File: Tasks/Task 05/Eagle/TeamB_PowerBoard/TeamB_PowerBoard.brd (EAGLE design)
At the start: 100 x 63.5 mm, 35 parts

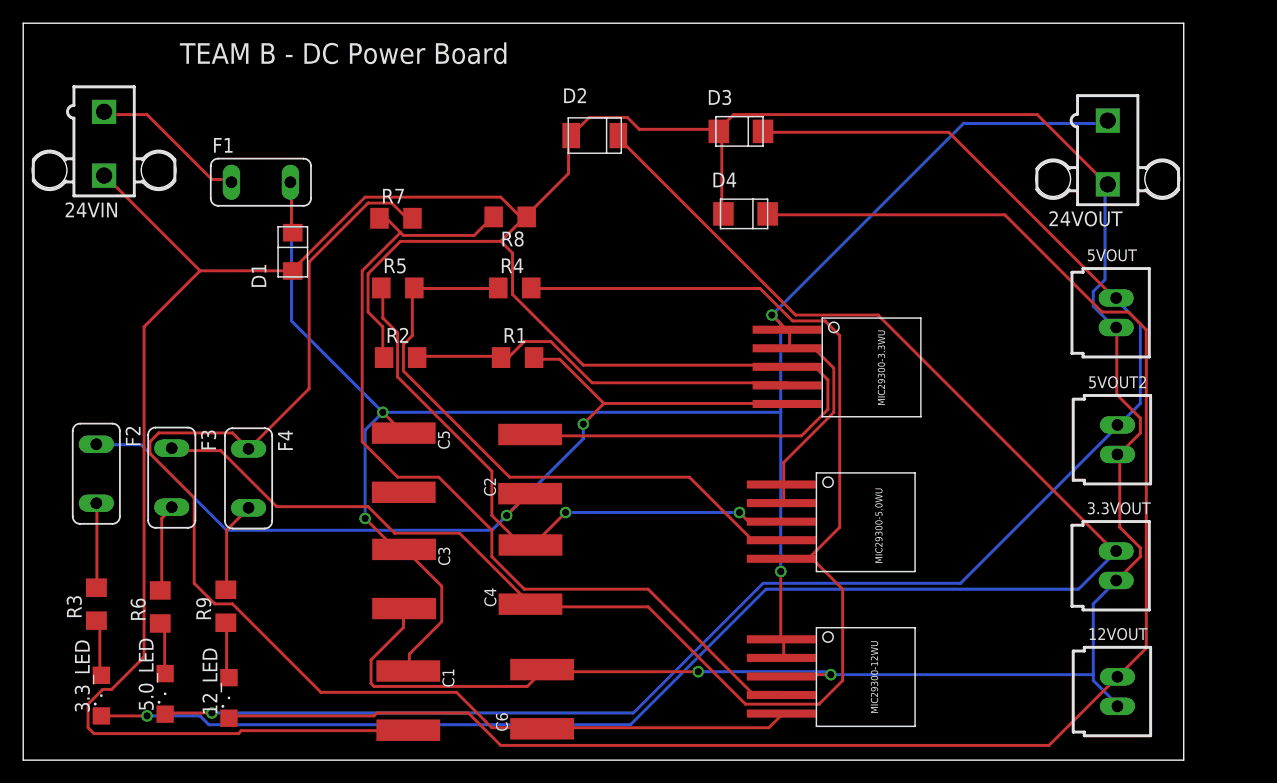
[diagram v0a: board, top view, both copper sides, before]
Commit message: Added the 4 holes to the PCB
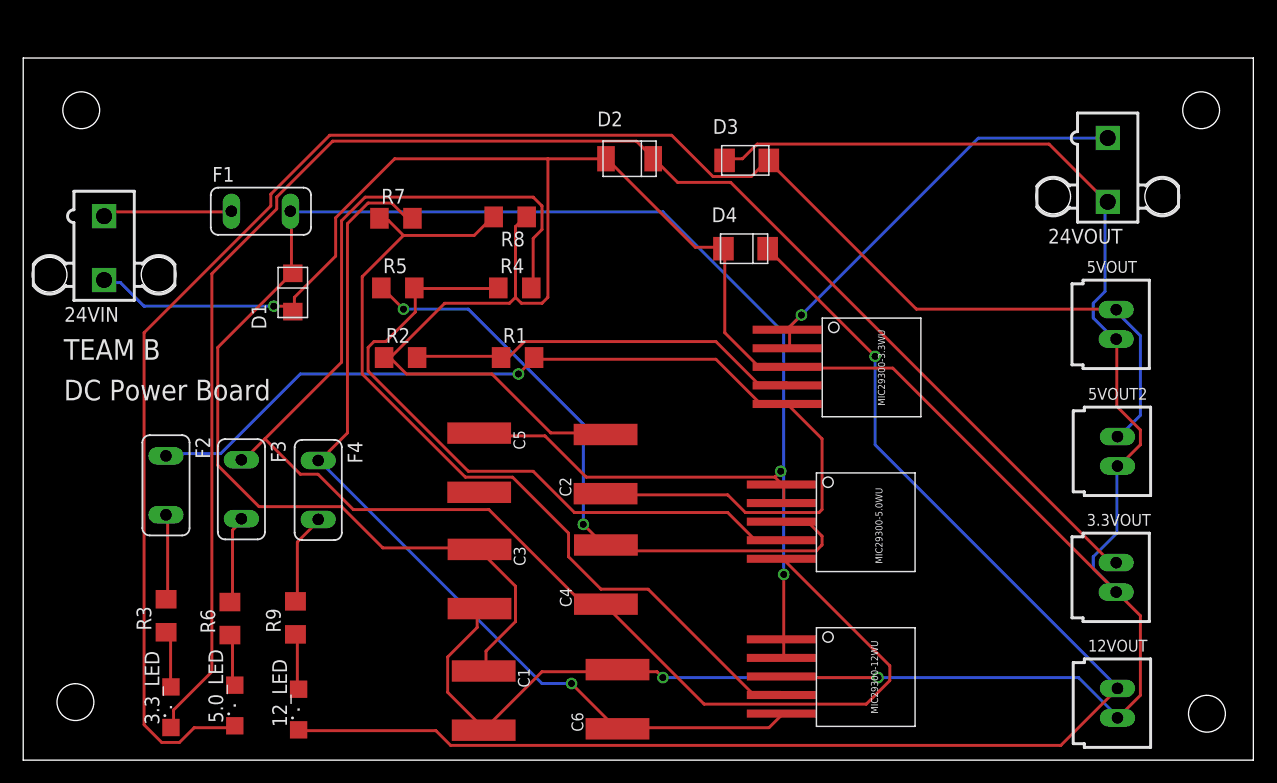
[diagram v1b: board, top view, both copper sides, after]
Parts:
- moved 24VIN 9.00 mm to (6.97, 44.1)
- moved C1 6.50 mm to (39.7, 5.13)
- moved C2 6.50 mm to (50.2, 25.5)
- moved C3 6.50 mm to (39.3, 15.6)
- moved C4 6.50 mm to (50.2, 16.0)
- moved C5 6.50 mm to (39.3, 25.6)
- moved C6 6.50 mm to (51.2, 5.25)
- moved F2 6.08 mm to (12.3, 23.7)
- moved R3 6.08 mm to (12.3, 12.4)
- moved 12_LED 6.08 mm to (23.7, 4.36)
- moved 3.3_LED 6.08 mm to (12.7, 4.56)
- moved 5.0_LED 6.08 mm to (18.2, 4.71)
- moved F3 6.08 mm to (18.8, 23.3)
- moved F4 6.08 mm to (25.4, 23.3)
- moved R6 6.08 mm to (17.8, 12.2)
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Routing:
- net GND: track 396.0 -> 341.0 mm, vias 2 -> 3
- net N$8: track 109.4 -> 78.5 mm, vias 0 -> 1
- net N$1: track 180.0 -> 207.6 mm, vias 4 -> 3
- net N$18: track 148.1 -> 123.5 mm, vias 0 -> 1
- net N$9: track 151.8 -> 138.9 mm, vias 1 -> 0
- net N$15: track 141.5 -> 154.3 mm, vias 1 -> 0
- net N$5: track 78.3 -> 88.5 mm, vias 2 -> 1
- net N$6: track 51.1 -> 57.5 mm
- net N$13: track 53.5 -> 58.3 mm
- net N$7: track 133.0 -> 128.8 mm
- net N$19: track 77.2 -> 73.5 mm
- net VCC: track 13.6 -> 11.1 mm
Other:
- board size 100 x 63.5 mm -> 106 x 60.5 mm
- board text added: "DC Power Board"
- board text added: "TEAM B"
- board text removed: "TEAM B - DC Power Board"

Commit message: Added 4th LED
Added 4th LED to PCB and Schematic
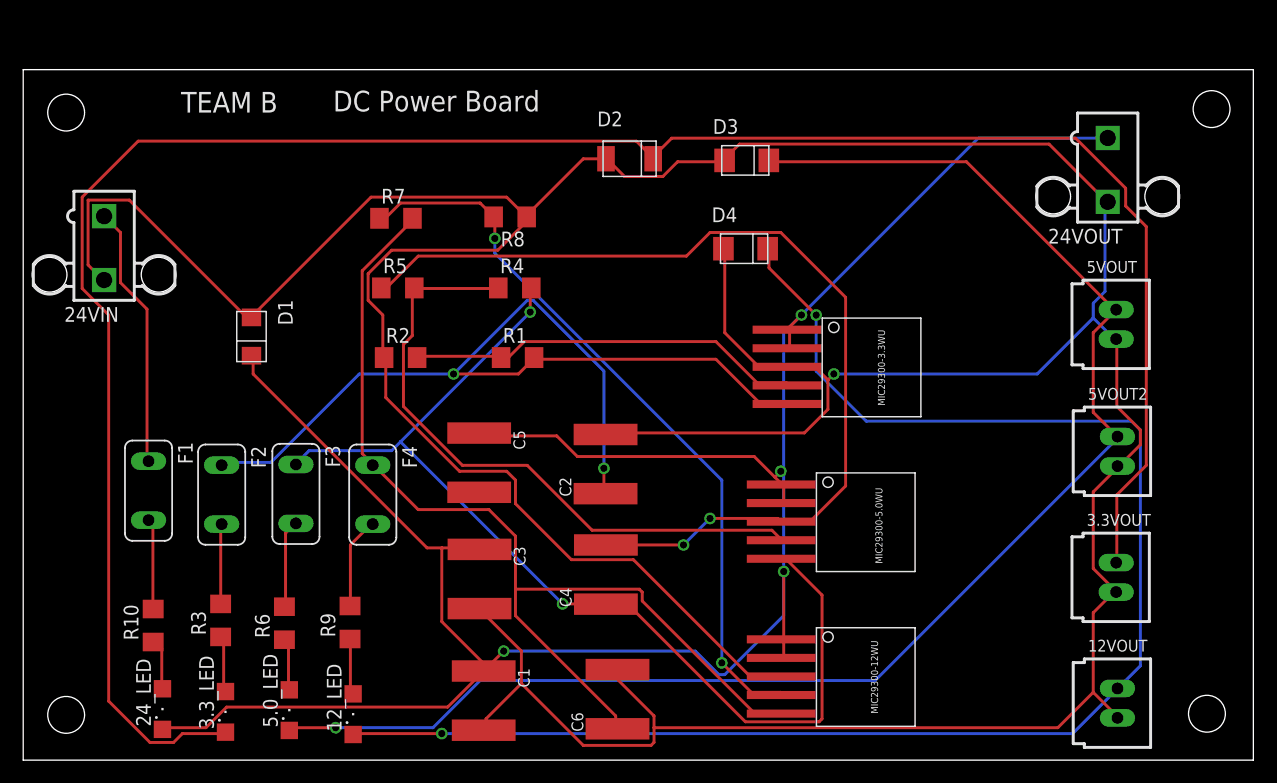
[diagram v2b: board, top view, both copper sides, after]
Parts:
- added 24_LED: (no value), led:SML1206
- added R10: 2.2K, rcl:R1206
- moved F1 26.0 mm to (10.8, 23.2), turned to 270 degrees
- moved F2 4.87 mm to (17.1, 22.9)
- moved R6 4.72 mm to (22.5, 11.8)
- moved R3 4.72 mm to (17.0, 12.0)
- moved 12_LED 4.72 mm to (28.4, 3.96)
- moved 3.3_LED 4.72 mm to (17.4, 4.16)
- moved 5.0_LED 4.72 mm to (22.9, 4.31)
- moved F3 4.72 mm to (23.5, 22.9)
- moved F4 4.72 mm to (30.1, 22.9)
- moved R9 4.72 mm to (28.2, 11.9)
- moved D1 4.09 mm to (19.7, 37.4), turned to 270 degrees
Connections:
- new net N$10: F1.2, R10.2
- new net N$20: 24_LED.A, R10.1
- net N$1: now also 24_LED.C; no longer F1.2
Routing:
- net N$9: track 138.9 -> 185.5 mm
- net N$7: track 128.8 -> 89.9 mm, vias 0 -> 2
- net GND: track 341.0 -> 373.6 mm, vias 3 -> 1
- net N$6: track 57.5 -> 83.6 mm
- net N$15: track 154.3 -> 129.9 mm, vias 0 -> 1
- net VCC: track 11.1 -> 22.7 mm
- net N$19: track 73.5 -> 63.8 mm, vias 0 -> 2
- net N$18: track 123.5 -> 133.0 mm, vias 1 -> 2
- net N$8: track 78.5 -> 86.3 mm, vias 1 -> 0
- net N$10: track 0.00 -> 7.82 mm
- net N$1: track 207.6 -> 200.2 mm, vias 3 -> 4
- net N$5: track 88.5 -> 83.0 mm, vias 1 -> 2
- net N$20: track 0.00 -> 4.46 mm
- net N$13: track 58.3 -> 55.3 mm
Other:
- board size 106 x 60.5 mm -> 106 x 59.5 mm

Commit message: Fixed Libraries and Wiring
Fixed the Library components to reflect DIP variants.
Fixed schematic for LED wiring.
ERC passes for both PCB and SCH
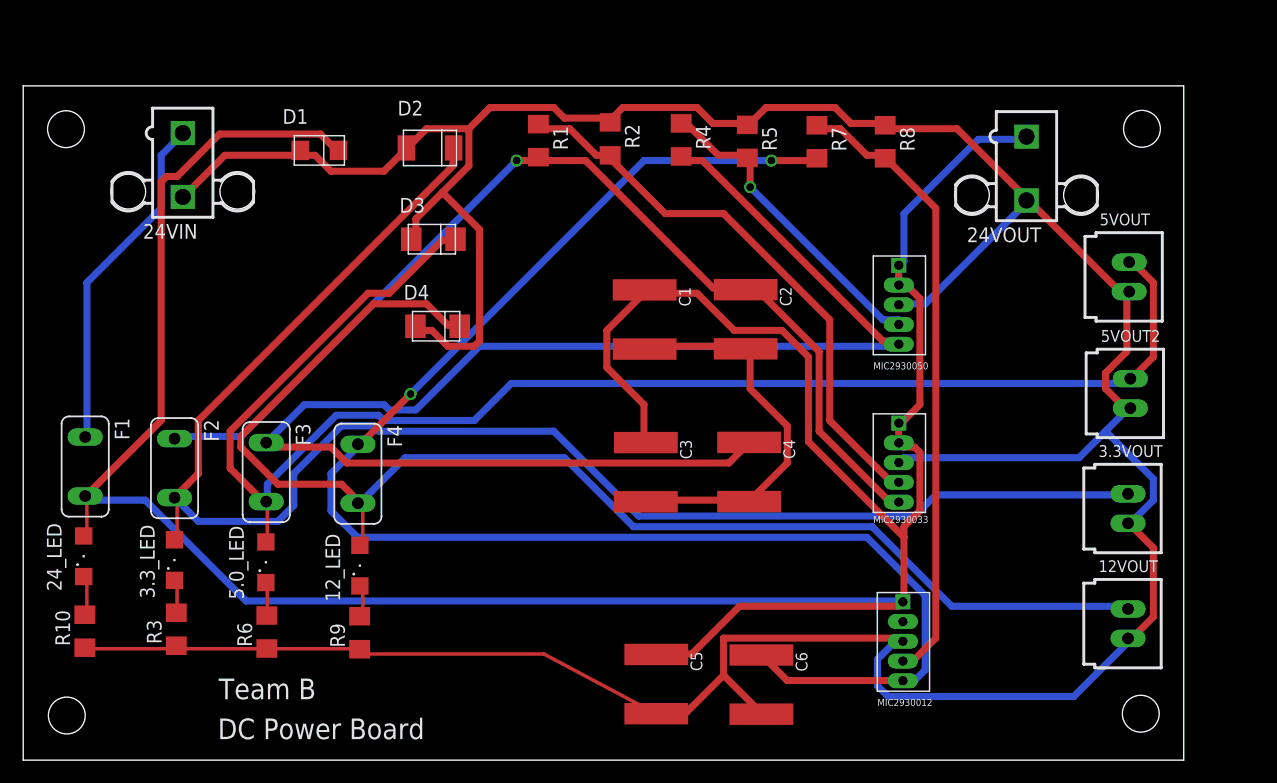
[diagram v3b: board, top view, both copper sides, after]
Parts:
- F1: value (none) -> 15A
- F2, F3, F4: value (none) -> 4.5A
- R1, R4, R7: value 180 -> 1k
- R2: value 180 -> 1.69k
- R5: value 180 -> 3k
- R8: value 180 -> 8.66k
- U$1: device MIC2930033WU:MIC29300W -> MIC2930033WU:MIC29300WU
- U$2: device MIC2930050WU:MIC29300W -> MIC2930050WU:MIC29300WU
- U$3: device MIC2930012WU:MIC29300W -> MIC2930012WU:MIC29300WU
- moved R7 36.9 mm to (68.4, 53.3), turned to 270 degrees
- moved C1 35.6 mm to (53.5, 38.0)
- moved R8 33.0 mm to (74.3, 53.3), turned to 270 degrees
- moved R5 32.7 mm to (62.4, 53.3), turned to 270 degrees
- moved D3 27.8 mm to (34.2, 44.9)
- moved D4 27.4 mm to (34.6, 37.4)
- moved R2 26.1 mm to (50.6, 53.5), turned to 270 degrees
- moved C5 24.4 mm to (54.5, 6.55)
- moved R4 19.2 mm to (56.7, 53.4), turned to 270 degrees
- moved R1 18.8 mm to (44.4, 53.4), turned to 270 degrees
- moved C2 17.4 mm to (62.2, 38.0), turned to 270 degrees
- moved U$1 17.3 mm to (73.2, 21.3), turned to 0 degrees
- moved D2 17.2 mm to (35.0, 52.8)
- moved C3 17.0 mm to (53.6, 24.8)
- moved D1 15.9 mm to (24.6, 52.5), turned to 0 degrees
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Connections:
- removed net N$14: 5.0_LED.A, R6.1
- removed net N$15: 5.0_LED.C, 5VOUT.1, 5VOUT2.1, D3.2
- removed net N$16: F4.2, R9.2
- removed net N$17: 12_LED.A, R9.1
- removed net N$18: 12VOUT.1, 12_LED.C, D4.2
- removed net N$20: 24_LED.A, R10.1
- net GND: now also C4.2, C5.2, R10.1, R3.1, R5.1, R6.1, R9.1, U$1.GND, U$2.GND, U$3.GND; no longer U$1.P$3, U$3.P$3
- net N$1: now also 24_LED.A, F1.2, U$1.EN, U$1.VIN, U$2.EN, U$2.VIN, U$3.VIN; no longer 24_LED.C, U$1.P$1, U$1.P$2, U$2.P$1, U$2.P$2, U$3.P$1, U$3.P$2
- net N$10: now also 12_LED.C, R9.2; no longer F1.2, R10.2
- net N$11: now also 3.3_LED.C, R3.2; no longer F3.2, R6.2
- net N$12: now also U$1.ADJ; no longer U$1.P$4
- net N$13: now also U$2.ADJ; no longer U$2.P$4
- net N$19: now also U$3.ADJ; no longer U$3.P$4
- net N$2: now also 5.0_LED.C, R6.2; no longer C5.2
- net N$3: now also 24_LED.C, R10.2; no longer F2.2, R3.2
- net N$4: now also 5.0_LED.A, 5VOUT.1, 5VOUT2.1, D3.2, F3.2; no longer 3.3_LED.A, R3.1
- net N$5: now also U$1.VOUT; no longer U$1.P$5
- net N$6: now also 12VOUT.1, 12_LED.A, D4.2, F4.2; no longer C4.2, R5.1, U$2.P$3
- net N$7: now also U$2.VOUT; no longer U$2.P$5
- net N$8: now also U$3.VOUT; no longer U$3.P$5
- net N$9: now also 3.3_LED.A, F2.2; no longer 3.3_LED.C
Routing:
- net N$18: track 133.0 -> 0.00 mm, vias 2 -> 0
- net N$15: track 129.9 -> 0.00 mm, vias 1 -> 0
- net N$4: track 4.87 -> 129.8 mm
- net N$1: track 200.2 -> 251.1 mm, vias 4 -> 0
- net N$9: track 185.5 -> 136.2 mm
- net N$8: track 86.3 -> 132.4 mm, vias 0 -> 2
- net N$7: track 89.9 -> 127.3 mm, vias 2 -> 0
- net N$6: track 83.6 -> 115.3 mm, vias 2 -> 0
- net GND: track 373.6 -> 345.6 mm, vias 1 -> 0
- net N$13: track 55.3 -> 27.5 mm, vias 0 -> 1
- net N$12: track 34.2 -> 49.2 mm
- net N$19: track 63.8 -> 54.0 mm, vias 2 -> 0
- net N$16: track 7.93 -> 0.00 mm
- net VCC: track 22.7 -> 29.7 mm
- net N$5: track 83.0 -> 89.0 mm, vias 2 -> 1
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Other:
- board size 106 x 59.5 mm -> 100 x 58.1 mm
- board text added: "Team B"
- board text removed: "TEAM B"

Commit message: Changes to PCB layout and added 2D drawing
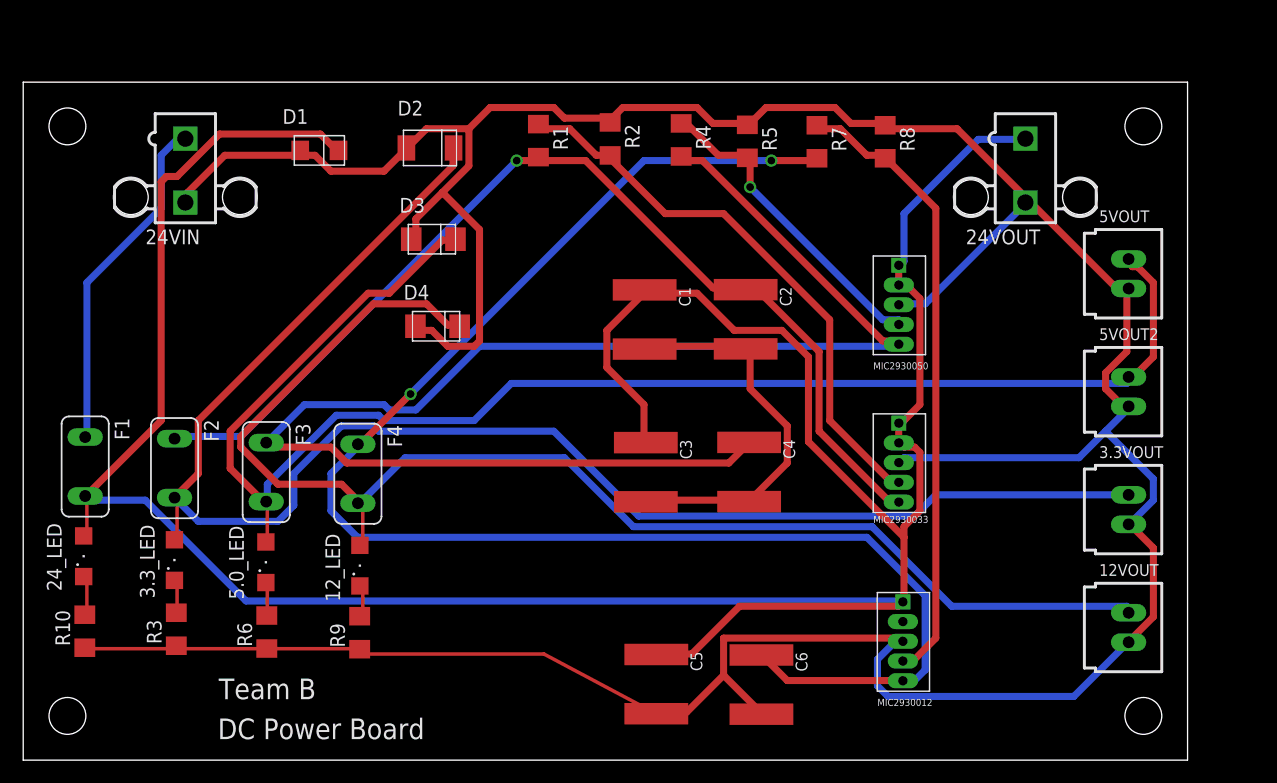
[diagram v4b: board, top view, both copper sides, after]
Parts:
- moved 24VIN 0.53 mm to (14.0, 50.8)
- moved 12VOUT 0.33 mm to (95.2, 11.4)
- moved 5VOUT 0.27 mm to (95.2, 41.9)
- moved 5VOUT2 0.21 mm to (95.2, 31.8)
- moved 24VOUT 0.20 mm to (86.4, 50.8)
- moved 3.3VOUT 0.10 mm to (95.2, 21.6)
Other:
- board size 100 x 58.1 mm -> 100.3 x 58.4 mm
